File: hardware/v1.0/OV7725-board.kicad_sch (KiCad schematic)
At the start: 24 parts, among them J11 Conn_01x04, J12 Conn_01x34, J13 Conn_02x10_Odd_Even, U11 TLV62585, U12 CH32V003JxMx, Y2 TFOM24M4RHKCNT2T

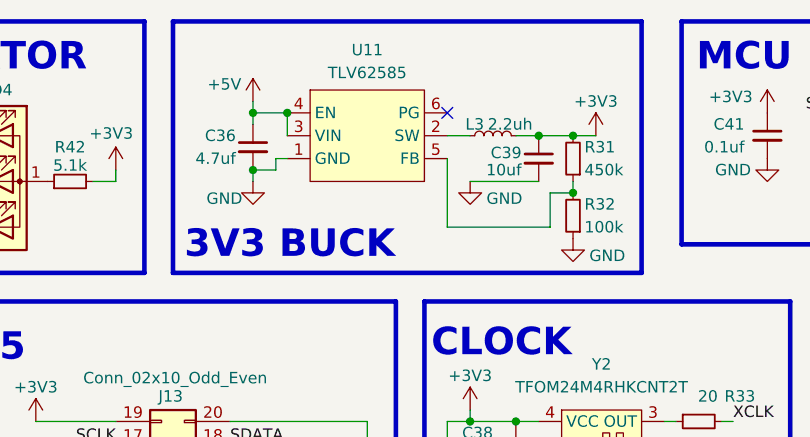
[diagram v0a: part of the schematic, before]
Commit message: redoing 3v3 regulators
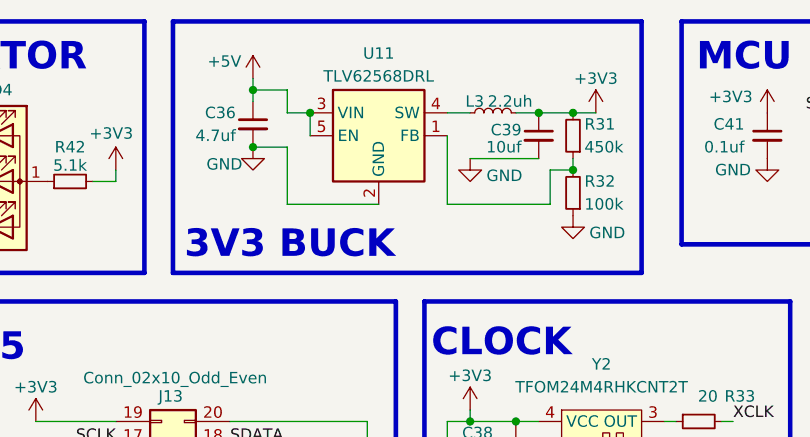
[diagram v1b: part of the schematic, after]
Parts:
- removed U11: TLV62585, Package_TO_SOT_SMD:SOT-563, symbol mylib:TLV62585
- added U11: TLV62568DRL, Package_TO_SOT_SMD:SOT-563, symbol Regulator_Switching:TLV62568DRL
- C36, C39: footprint Capacitor_SMD:C_0805_2012Metric -> Capacitor_SMD:C_0603_1608Metric
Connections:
- net +5V: now also U11.3 (VIN), U11.5 (EN)
- net GND: now also U11.2 (GND)
- net at L3.1: now also U11.4 (SW)
- net at R31.1, R32.2: now also U11.1 (FB)
- no-connect marks 23 -> 22
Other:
- moved on the sheet: C36, C39, L3, R31, R32

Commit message: finished mainboard + progress on peripherals
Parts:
- Y2: footprint (none) -> mylib:TFOM24M4RHKCNT2T
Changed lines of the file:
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@@
 			)
 		)
-		(property "Footprint" ""
+		(property "Footprint" "mylib:TFOM24M4RHKCNT2T"
 			(at 142.24 60.96 0)
 			(effects

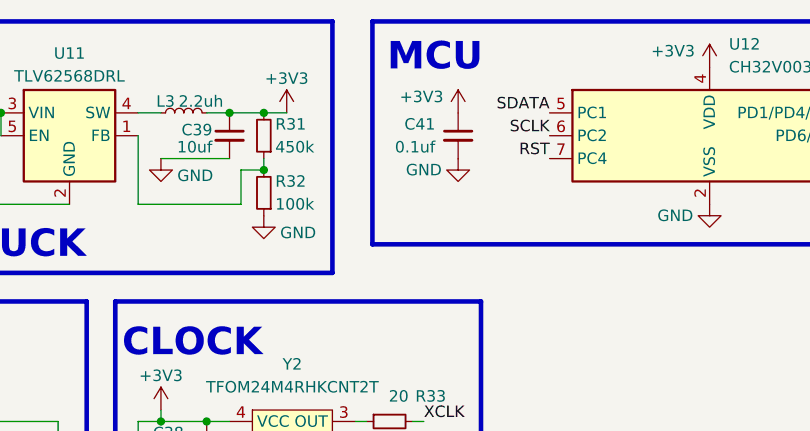
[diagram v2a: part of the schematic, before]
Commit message: added tvs diode+changed inductors
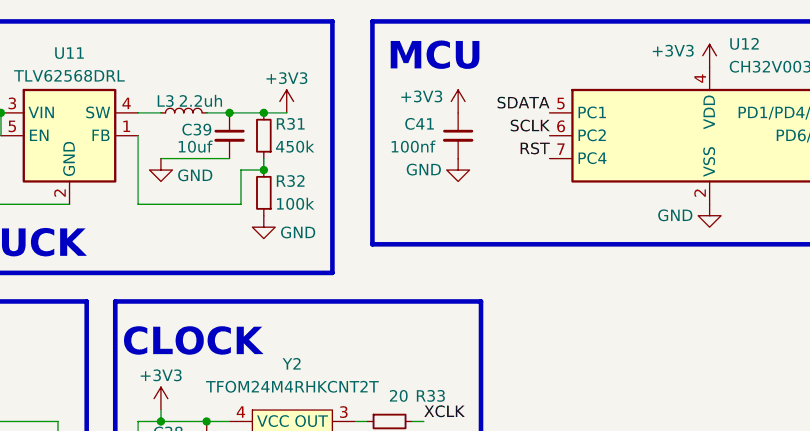
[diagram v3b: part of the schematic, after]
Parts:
- C41: value 0.1uf -> 100nf
- L3: footprint Inductor_SMD:L_0603_1608Metric -> Inductor_SMD:L_0805_2012Metric
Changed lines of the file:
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@@
 			)
 		)
-		(property "Footprint" "Inductor_SMD:L_0603_1608Metric"
+		(property "Footprint" "Inductor_SMD:L_0805_2012Metric"
 			(at 129.54 24.13 0)
 			(effects
@@
 			)
 		)
-		(property "Value" "0.1uf"
+		(property "Value" "100nf"
 			(at 157.48 27.94 0)
 			(effects
